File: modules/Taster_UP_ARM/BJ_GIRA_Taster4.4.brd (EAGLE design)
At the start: 52.9 x 50 mm, 68 parts, among them IC1 LPC1115, IC100 BD9G101, T1 BC856, T2 BCP52, T3 BC847

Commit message: naechster Vorschlag
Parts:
- removed LED1: (no value), led:LED3MM
- removed R18: 3k3, rcl:R1206
- added JP1: J, pinhead-2:2X05M
- moved R23 90.9 mm to (8.81, 25.9)
- moved R22 85.9 mm to (8.65, 22.6)
- moved C13 84.9 mm to (11.4, 18.8), turned to 180 degrees
- moved C14 76.1 mm to (12.7, 17.1), flipped to the bottom, turned to 180 degrees
- moved C7 69.9 mm to (12.7, 19.7), flipped to the bottom
- moved R7 67.2 mm to (75.7, 62.5), flipped to the bottom
- moved T1 67.1 mm to (11.3, 30.2), turned to 270 degrees
- moved R6 59.8 mm to (63.4, 63.3), turned to 270 degrees
- moved R16 57.1 mm to (33.6, 8.65)
- moved R101 54.5 mm to (43.7, 44.3), flipped to the bottom
- moved D7 53.7 mm to (6.75, 33.1), turned to 90 degrees
- moved C1 45.3 mm to (5.79, 34.2), flipped to the bottom, turned to 270 degrees
- moved C104 43.6 mm to (45.1, 47.0), flipped to the bottom, turned to 180 degrees
- moved R10 42.4 mm to (66.5, 68.4), flipped to the bottom, turned to 90 degrees
- moved R11 41.1 mm to (69.6, 62.8), turned to 90 degrees
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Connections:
- removed net INT0: R18.2
- removed net VCC: R14.1, R18.1
- new net N$15: JP1.3
- new net N$20: JP1.4
- new net N$21: JP1.8
- new net N$22: JP1.7
- net +3V3: now also R14.1
- net EXT11: now also JP1.10, R1.1
- net EXT14: now also JP1.1
- net EXT7: now also S1.P$1
- net GND: now also JP1.5; no longer LED1.K
- net IO15: now also JP1.9
- net IO2: now also JP1.2; no longer S1.P$1
- net N$8: now also JP1.6; no longer LED1.A

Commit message: vorschlag Erweiterungsstecker
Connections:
- removed net N$15: JP1.3
- removed net N$20: JP1.4
- removed net N$21: JP1.8
- removed net N$22: JP1.7
- net +3V3: now also JP1.4
- net EXT5: now also JP1.7
- net EXT6: now also JP1.8
- net IO4: now also JP1.3
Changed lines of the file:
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@@
 <signal name="IO4">
 <contactref element="IC1" pad="31"/>
+<contactref element="JP1" pad="3"/>
+<wire x1="11.283125" y1="31.12875" x2="31.00375" y2="28.00375" width="0" layer="19" extent="16-16"/>
 </signal>
 <signal name="+3V3">
@@
 <contactref element="C15" pad="2"/>
 <contactref element="R14" pad="1"/>
+<contactref element="JP1" pad="4"/>
 <wire x1="13.861875" y1="74.850625" x2="16.83425" y2="77.231875" width="0" layer="19" extent="1-1"/>
 <wire x1="12.195" y1="70.564375" x2="13.861875" y2="74.850625" width="0" layer="19" extent="1-1"/>
@@
 <wire x1="15.333125" y1="26.07875" x2="10.232625" y2="25.87625" width="0" layer="19" extent="1-16"/>
 <wire x1="12.931375" y1="34.13125" x2="15.333125" y2="26.07875" width="0" layer="19" extent="1-16"/>
+<wire x1="29.00375" y1="28.00375" x2="15.333125" y2="26.07875" width="0" layer="19" extent="16-16"/>
 </signal>
 <signal name="IO16">
@@
 <signal name="EXT6">
 <contactref element="IC1" pad="18"/>
+<contactref element="JP1" pad="8"/>
+<wire x1="6.733125" y1="26.57875" x2="29.00375" y2="32.00375" width="0" layer="19" extent="16-16"/>
 </signal>
 <signal name="EXT5">
 <contactref element="IC1" pad="21"/>
+<contactref element="JP1" pad="7"/>
+<wire x1="6.733125" y1="28.07875" x2="31.00375" y2="32.00375" width="0" layer="19" extent="16-16"/>
 </signal>
 <signal name="EXT3">
@@
 <wire x1="14.1895" y1="44.1486" x2="18.703125" y2="42.08495" width="0" layer="19" extent="1-16"/>
 </signal>
-<signal name="N$15">
-<contactref element="JP1" pad="3"/>
-</signal>
-<signal name="N$20">
-<contactref element="JP1" pad="4"/>
-</signal>
-<signal name="N$21">
-<contactref element="JP1" pad="8"/>
-</signal>
-<signal name="N$22">
-<contactref element="JP1" pad="7"/>
-</signal>
 </signals>

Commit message: weiter geroutet...
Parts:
- moved R7 53.6 mm to (46.2, 17.7)
- moved T3 53.4 mm to (44.5, 22.5)
- moved R5 52.8 mm to (49.3, 21.4)
- moved R4 52.7 mm to (49.2, 23.9)
- moved R2 52.6 mm to (44.2, 26.4)
- moved T2 52.6 mm to (44.2, 32.5)
- moved R3 51.4 mm to (50.6, 28.3)
- moved C2 48.4 mm to (39.5, 30.5), turned to 90 degrees
- moved R10 46.7 mm to (36.0, 33.1), turned to 0 degrees
- moved C3 41.3 mm to (43.0, 43.7), turned to 0 degrees
- moved R6 40.6 mm to (41.3, 29.4), turned to 180 degrees
- moved S5 32.9 mm to (30.1, 15.1), turned to 0 degrees
- moved R12 32.7 mm to (37.2, 50.6)
- moved C1 30.6 mm to (36.0, 29.3), turned to 0 degrees
- moved C15 29.9 mm to (30.7, 51.1)
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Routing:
- net +3V3: track 0.00 -> 107.5 mm, vias 0 -> 4
- net EIB_DC: track 0.00 -> 72.6 mm, vias 0 -> 3
- net EIB_IN: track 0.00 -> 51.9 mm, vias 0 -> 3
- net RESET: track 0.00 -> 40.8 mm
- net BUS_V: track 0.00 -> 40.4 mm, vias 0 -> 3
- net SWCLK: track 0.00 -> 39.1 mm, vias 0 -> 2
- net GND: track 0.00 -> 38.6 mm, vias 0 -> 2
- net ISP_EN: track 0.00 -> 35.6 mm
- net REF: track 0.00 -> 33.5 mm, vias 0 -> 4
- net PROG: track 0.00 -> 31.0 mm, vias 0 -> 1
- net EIB+: track 0.00 -> 29.5 mm
- net ISP_TXD: track 0.00 -> 29.1 mm, vias 0 -> 2
- net SWDIO: track 0.00 -> 27.2 mm, vias 0 -> 1
- net N$11: track 0.00 -> 27.2 mm, vias 0 -> 1
- net ISP_RXD: track 0.00 -> 27.0 mm, vias 0 -> 2
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- added copper zone on layer 1, net GND
- added copper zone on layer 16, net GND

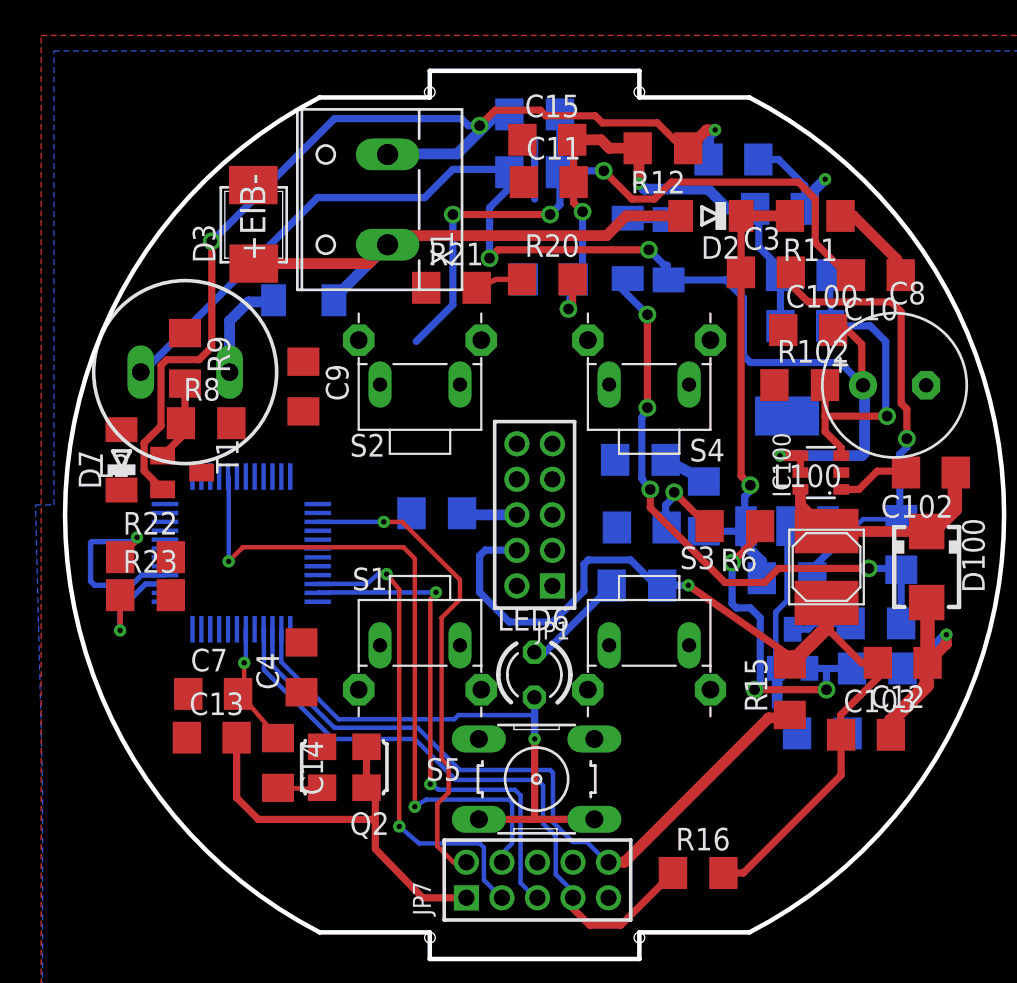
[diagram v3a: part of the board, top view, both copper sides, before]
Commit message: routing vorschlag alle gerouted, noch drc fehler
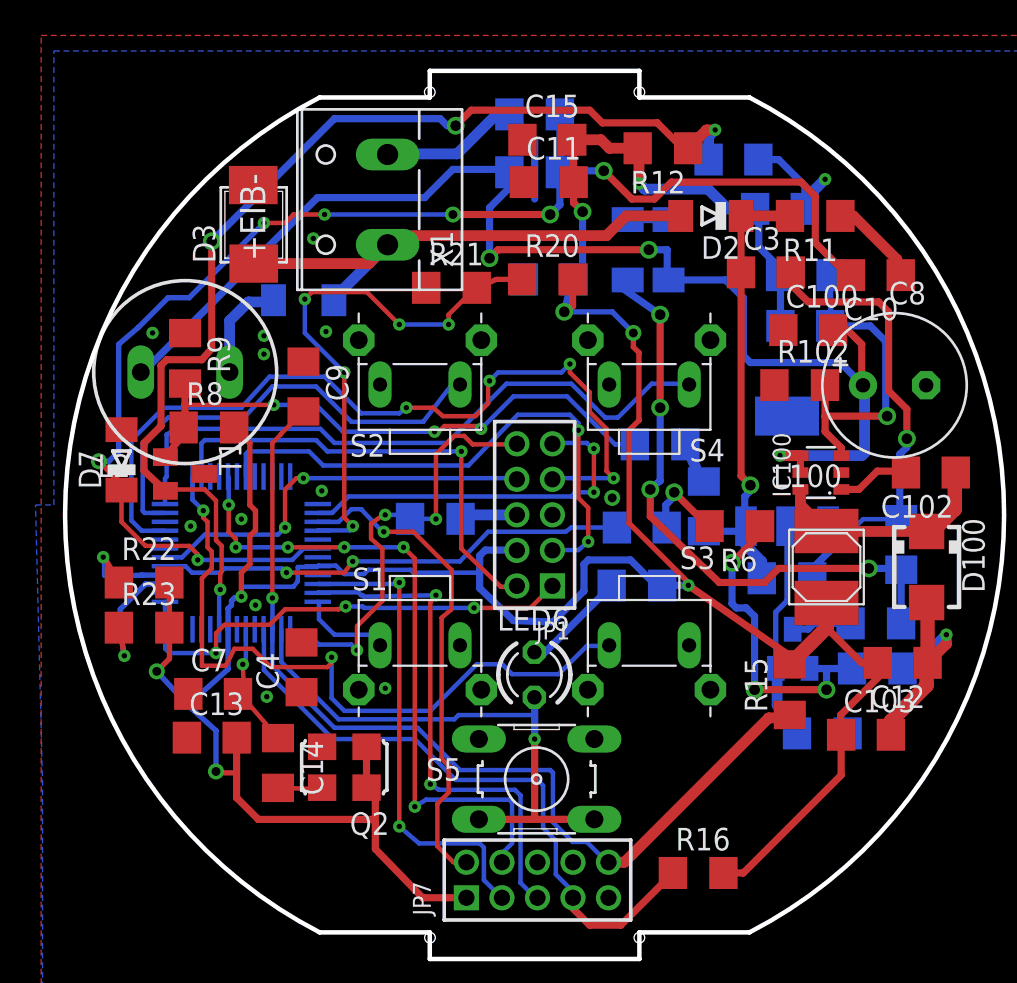
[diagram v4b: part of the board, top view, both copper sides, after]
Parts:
- moved R23 1.83 mm to (8.02, 23.7)
- moved R22 1.43 mm to (8.02, 26.2)
- moved R10 1.41 mm to (37.1, 34.0)
- moved R1 0.33 mm to (24.4, 29.8)
- moved R8 0.29 mm to (11.7, 34.9)
- moved T1 0.18 mm to (10.3, 32.3)
- moved D6 0.08 mm to (35.2, 44.9)
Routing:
- net +3V3: track 107.5 -> 176.8 mm, vias 4 -> 8
- net EXT5: track 0.00 -> 46.8 mm, vias 0 -> 4
- net EXT8: track 0.00 -> 40.3 mm, vias 0 -> 2
- net BUS_V: track 40.4 -> 78.0 mm, vias 3 -> 7
- net IO9: track 0.00 -> 36.8 mm
- net IO4: track 0.00 -> 30.9 mm, vias 0 -> 2
- net N$14: track 4.58 -> 32.5 mm, vias 0 -> 3
- net ID: track 2.65 -> 30.5 mm, vias 0 -> 5
- net EIB_OUT: track 0.00 -> 26.9 mm, vias 0 -> 2
- net EXT14: track 0.00 -> 26.8 mm, vias 0 -> 3
- net IO2: track 0.00 -> 26.3 mm, vias 0 -> 1
- net EXT4: track 0.00 -> 26.2 mm
- net EXT11: track 0.00 -> 25.2 mm, vias 0 -> 3
- net EXT6: track 0.00 -> 22.9 mm, vias 0 -> 2
- net IO15: track 0.00 -> 21.0 mm, vias 0 -> 2
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
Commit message: weiss nicht mehr...
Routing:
- net +3V3: track 176.8 -> 178.0 mm
- net IO2: track 26.3 -> 27.2 mm
- net GND: vias 14 -> 19

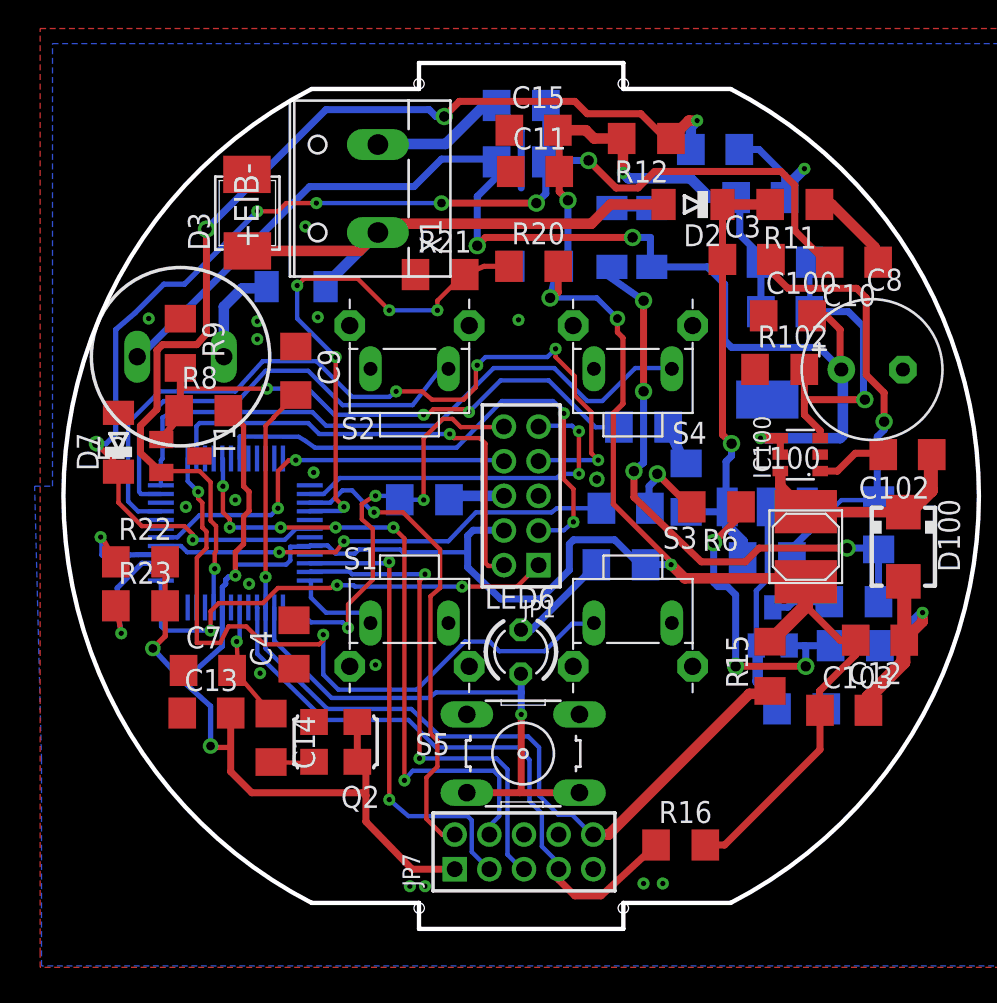
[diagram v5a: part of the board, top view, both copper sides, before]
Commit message: Paar Pauteile und vias verschoben
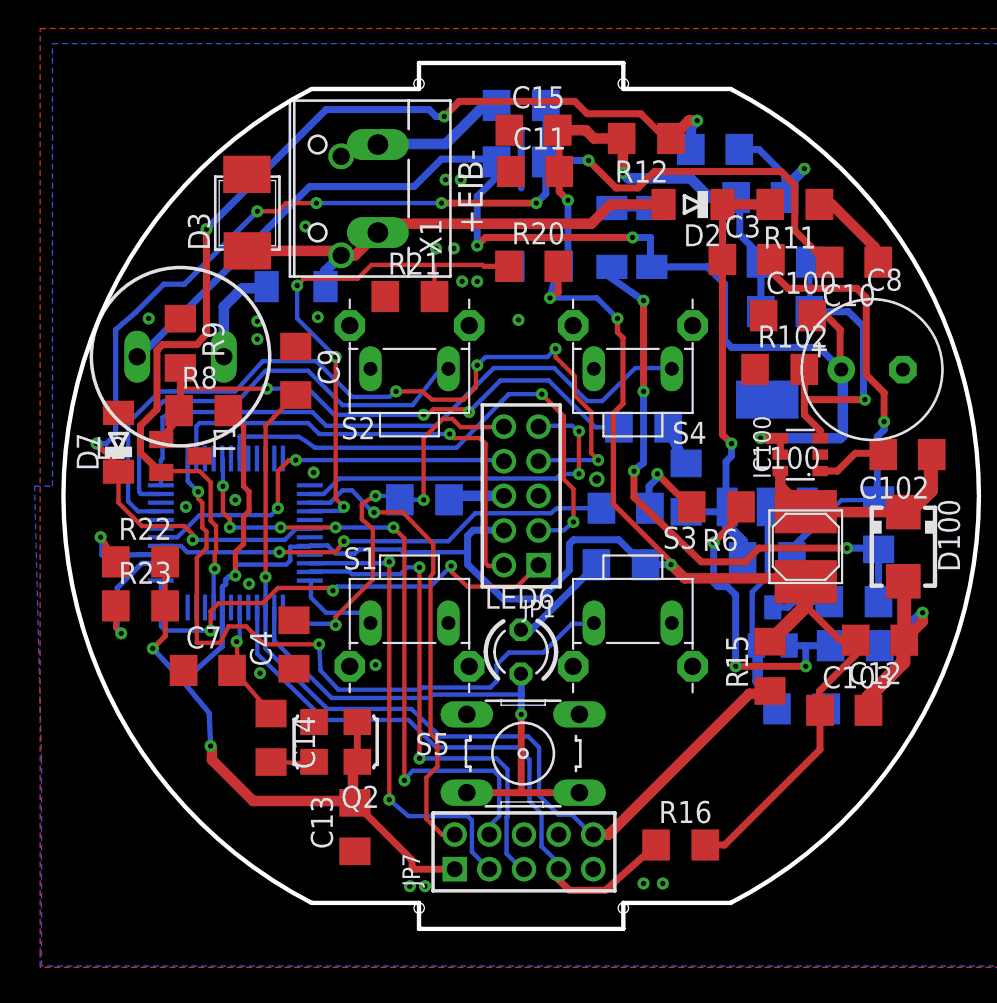
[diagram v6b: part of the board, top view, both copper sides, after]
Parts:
- moved C13 10.8 mm to (20.4, 10.9), turned to 90 degrees
- moved R21 2.16 mm to (23.6, 41.5)
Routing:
- net +3V3: track 178.0 -> 173.7 mm
- net EIB+: track 29.5 -> 27.5 mm, vias 0 -> 1
- net EXT14: track 26.8 -> 28.0 mm
- net EXT8: track 40.4 -> 39.5 mm
- net ID: track 30.5 -> 30.6 mm, vias 5 -> 3
- net GND: vias 19 -> 26

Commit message: finish optimiert
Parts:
- moved C103 2.59 mm to (49.8, 19.9)
- moved C102 1.14 mm to (51.3, 31.9)
- moved C12 1.07 mm to (49.9, 22.4)
- moved D100 0.95 mm to (51.1, 27.1)
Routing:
- net LX: track 12.8 -> 14.0 mm
- net GND: track 38.6 -> 37.5 mm, vias 26 -> 28
- net N$19: track 4.10 -> 3.45 mm
- net +3V3: track 173.7 -> 173.1 mm
